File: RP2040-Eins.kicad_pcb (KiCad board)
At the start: 4 copper layers, 68.6 x 53.3 mm, 61 parts, among them J1 CONN_PWR, J10 CONN_USB, J2 CONN_ICSP, J3 CONN_A, J4 CONN_P, J5 CONN_X, J7 CONN_JTAG, J8 CONN_D1, J9 CONN_D2, Q1 AO3401A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

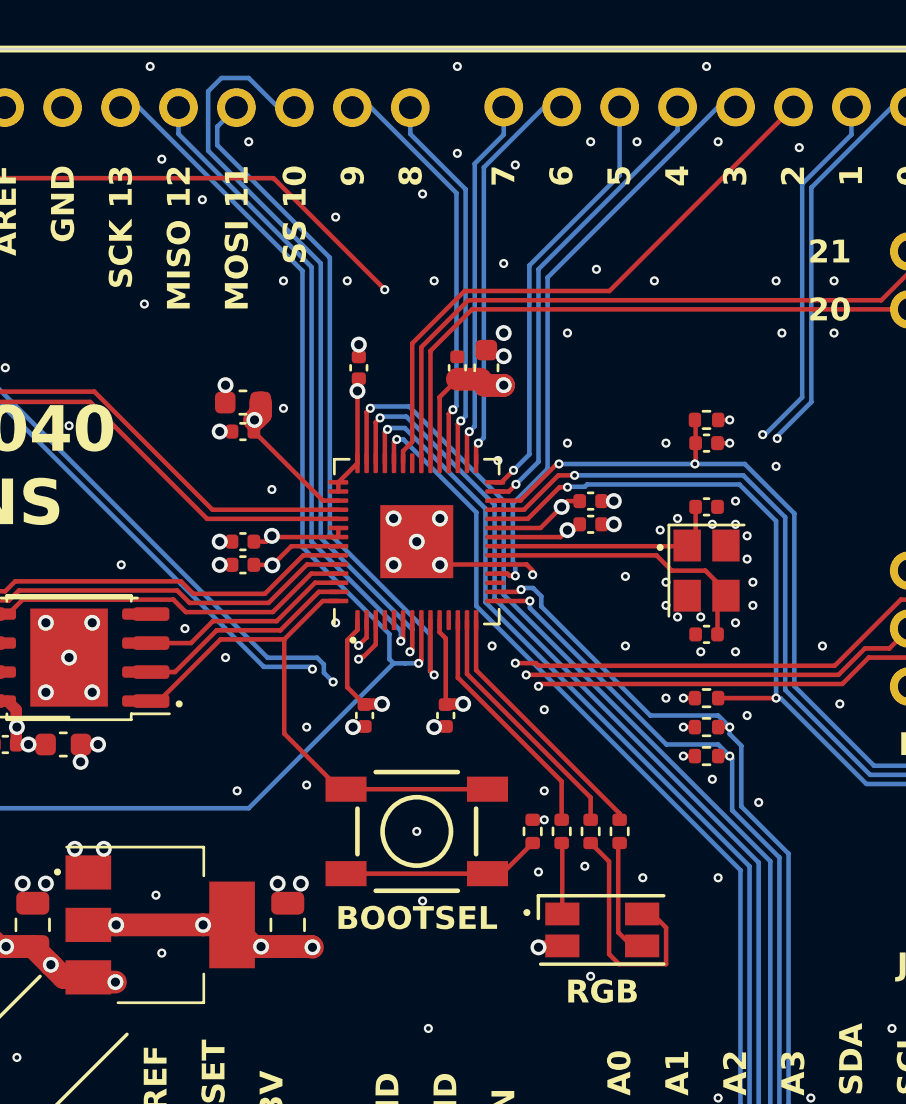
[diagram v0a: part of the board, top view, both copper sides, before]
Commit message: Added mosfets for RGB LED. Moved staff around.
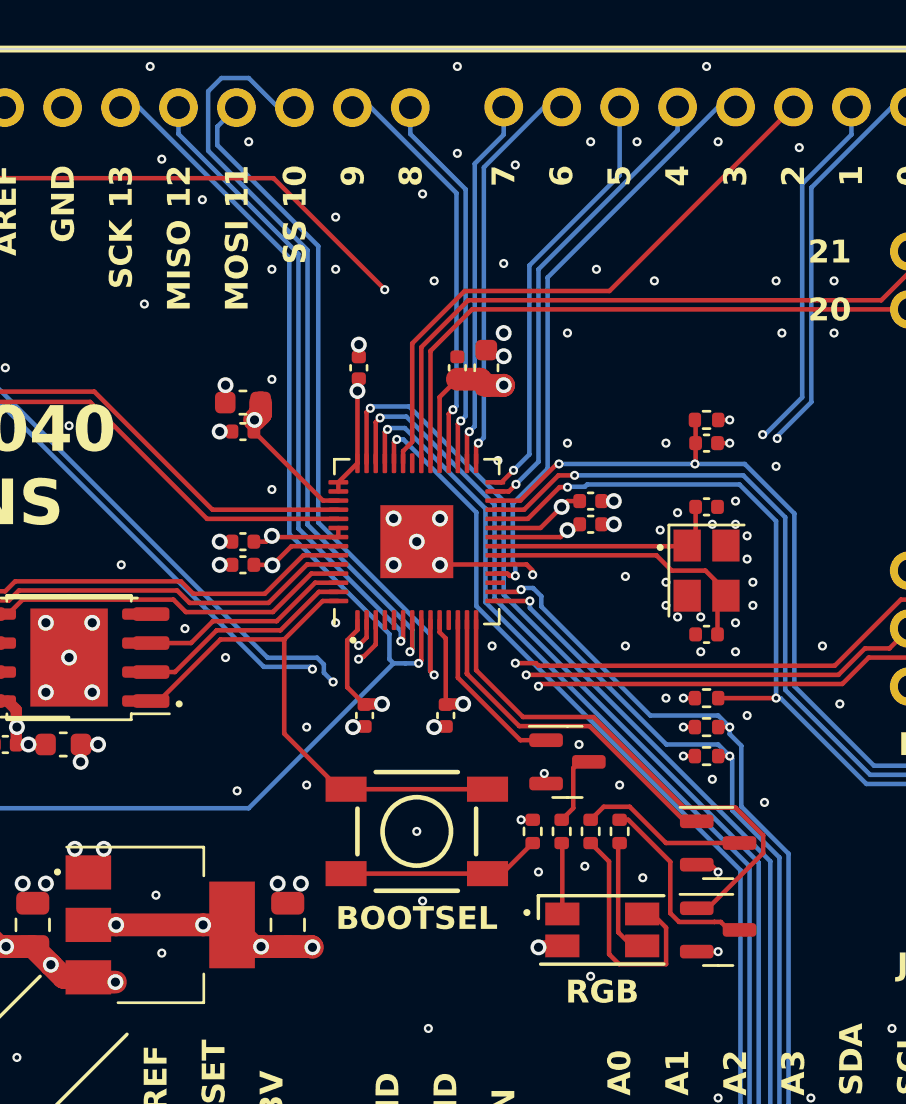
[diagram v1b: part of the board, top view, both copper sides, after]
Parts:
- added Q3: AO3400A, Package_TO_SOT_SMD:SOT-23, F.Cu at (175.5, 104.9)
- added Q4: AO3400A, Package_TO_SOT_SMD:SOT-23, F.Cu at (182.1, 108.5)
- added Q5: AO3400A, Package_TO_SOT_SMD:SOT-23, F.Cu at (182.1, 112.3)
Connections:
- R13 pad 1: LED_R -> Net-(Q3-D)
- R14 pad 1: LED_G -> Net-(Q4-D)
- R15 pad 1: LED_B -> Net-(Q5-D)
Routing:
- net LED_B: track 11.4 -> 22.2 mm
- net Net-(Q5-D): track 0.00 -> 8.57 mm
- net Net-(Q4-D): track 0.00 -> 7.42 mm
- net LED_G: track 11.0 -> 15.1 mm
- net Net-(Q3-D): track 0.00 -> 3.27 mm
- net LED_R: track 10.6 -> 7.53 mm
- net GND: track 10.7 -> 12.9 mm, vias 192 -> 194

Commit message: Moves few stuff around
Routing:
- net GND: vias 194 -> 195

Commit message: Moved stuff around.
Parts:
- moved Q2 22.8 mm to (162.3, 104.9), turned to 180 degrees
- turned Q5 to 180 degrees
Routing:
- net D13_SCK: track 90.6 -> 65.9 mm
- net Net-(D1-K): track 10.7 -> 33.2 mm, vias 0 -> 2
- net Net-(Q5-D): track 8.57 -> 6.70 mm
- net LED_B: track 22.2 -> 23.3 mm
- net GND: track 12.9 -> 13.9 mm, vias 195 -> 209

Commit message: Added QR Code on the back side.
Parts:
- added G***: LOGO, LOGO, B.Cu at (173.2, 114.0)

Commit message: Moved stuff around.
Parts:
- G1: renamed from G***; value LOGO -> QR-CODE
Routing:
- net GND: vias 209 -> 212

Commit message: Moved stuff around.
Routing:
- net GND: vias 212 -> 213
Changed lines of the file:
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@@
   (title_block
     (title "RP2040-Eins-0010")
-    (date "2023-11-03")
+    (date "2023-11-04")
     (rev "1.0")
     (company "(c) 2023 Andriy Golovnya")
@@
       (viasonmask false)
       (mode 1)
-      (useauxorigin false)
+      (useauxorigin true)
       (hpglpennumber 1)
       (hpglpenspeed 20)
@@
   (via (at 140.208 110.49) (size 0.7) (drill 0.4) (layers "F.Cu" "B.Cu") (free) (net 4))
   (via (at 179.834184 107.61333) (size 0.4) (drill 0.2) (layers "F.Cu" "B.Cu") (free) (net 4))
+  (via (at 171.45 103.505) (size 0.4) (drill 0.2) (layers "F.Cu" "B.Cu") (free) (net 4))
   (via (at 160.274 90.424) (size 0.7) (drill 0.4) (layers "F.Cu" "B.Cu") (free) (net 4))
   (via (at 156.464 121.412) (size 0.4) (drill 0.2) (layers "F.Cu" "B.Cu") (free) (net 4))
@@
   (segment (start 169.11 86.725686) (end 171.165687 84.67) (width 0.2) (layer "F.Cu") (net 30))
   (segment (start 169.11 91.8125) (end 169.11 86.725686) (width 0.2) (layer "F.Cu") (net 30))
+  (segment (start 136.0975 95.504) (end 135.795768 95.202268) (width 1) (layer "F.Cu") (net 31))
+  (segment (start 135.795768 91.735768) (end 135.636 91.576) (width 1) (layer "F.Cu") (net 31))
   (segment (start 134.420498 86.45) (end 133.585 86.45) (width 0.5) (layer "F.Cu") (net 31))
   (segment (start 136.67345 87.94455) (end 136.718 87.9) (width 0.5) (layer "F.Cu") (net 31))
   (segment (start 135.636 91.576) (end 135.41 91.35) (width 0.5) (layer "F.Cu") (net 31))
-  (segment (start 136.0975 95.504) (end 135.886 95.2925) (width 1) (layer "F.Cu") (net 31))
   (segment (start 135.41 91.35) (end 133.585 91.35) (width 0.5) (layer "F.Cu") (net 31))
   (segment (start 135.987982 87.94455) (end 136.67345 87.94455) (width 0.5) (layer "F.Cu") (net 31))
-  (segment (start 135.886 95.2925) (end 135.886 91.826) (width 1) (layer "F.Cu") (net 31))
+  (segment (start 135.795768 95.202268) (end 135.795768 91.735768) (width 1) (layer "F.Cu") (net 31))
   (segment (start 134.859502 86.889004) (end 134.420498 86.45) (width 0.5) (layer "F.Cu") (net 31))
-  (segment (start 135.886 91.826) (end 135.636 91.576) (width 1) (layer "F.Cu") (net 31))
   (segment (start 134.859502 87.0005) (end 134.859502 86.889004) (width 0.5) (layer "F.Cu") (net 31))
   (via (at 134.859502 87.0005) (size 0.7) (drill 0.4) (layers "F.Cu" "B.Cu") (net 31))
@@
         (xy 194.867834 119.916701)
         (xy 194.92561 119.65111)
-        (xy 194.945 119.38)
       )
     )
@@
         (xy 194.867834 91.976701)
         (xy 194.92561 91.71111)
-        (xy 194.945 91.44)
       )
     )
@@
         (xy 142.797834 124.996701)
         (xy 142.85561 124.73111)
-        (xy 142.875 124.46)
       )
     )
@@
         (xy 144.067834 76.736701)
         (xy 144.12561 76.47111)
-        (xy 144.145 76.2)
       )
     )

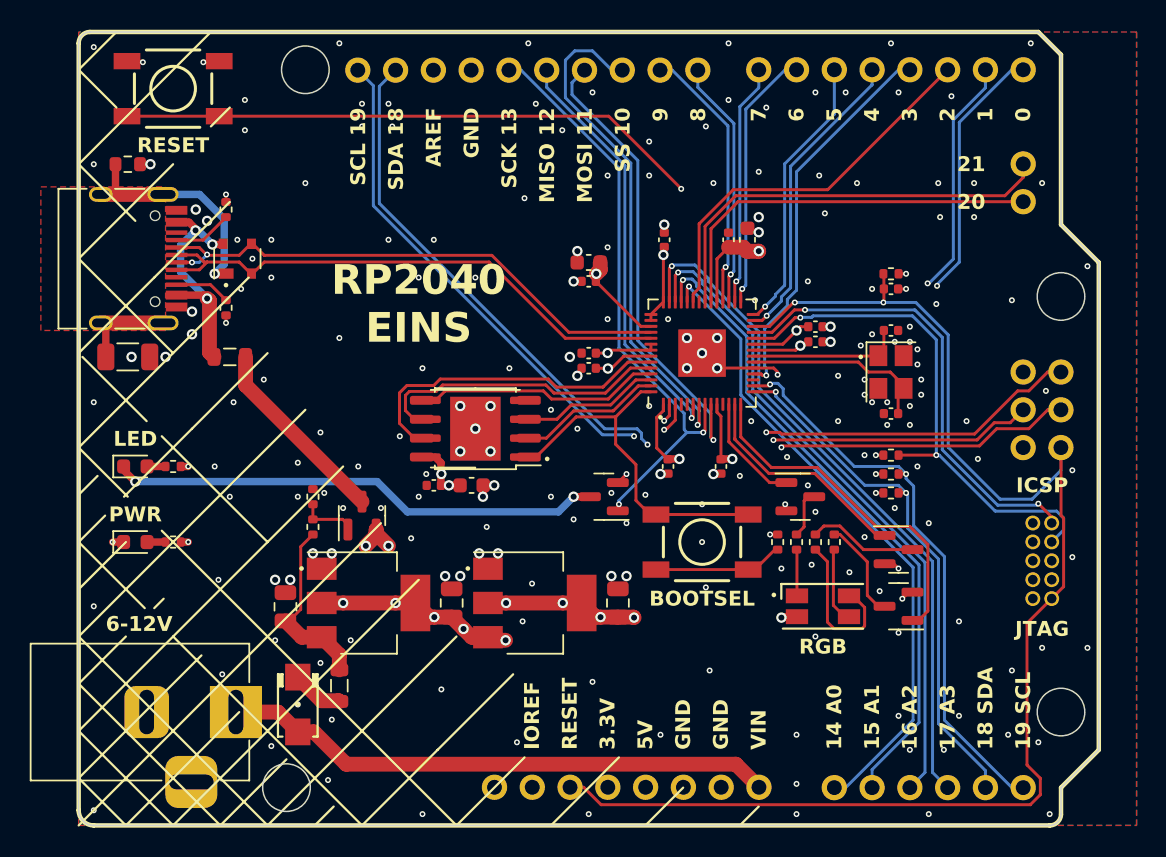
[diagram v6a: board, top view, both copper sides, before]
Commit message: Moved BOOTSEL button closer to the front edge of the board. Moved stuff around to fit better.
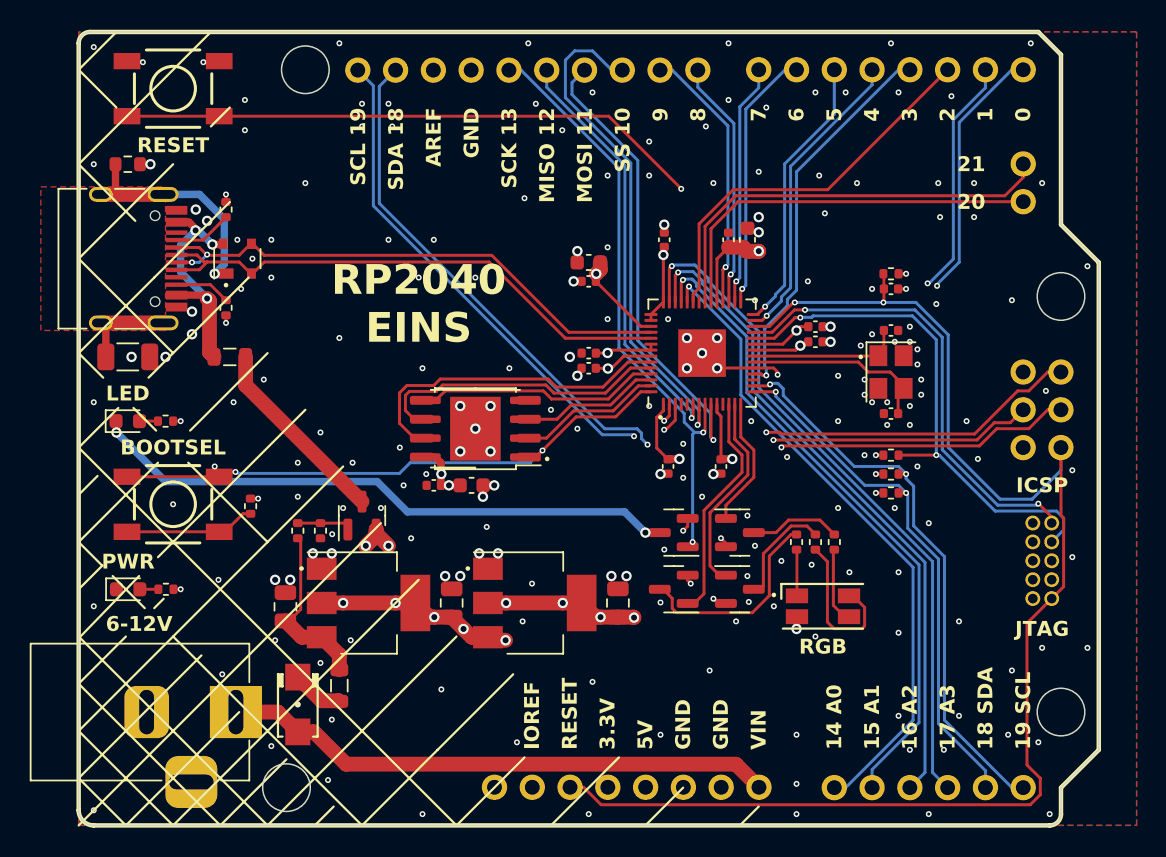
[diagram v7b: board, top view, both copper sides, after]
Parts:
- moved SW1 35.7 mm to (133.3, 105.4)
- moved R7 35.5 mm to (138.6, 105.5)
- moved Q5 11.8 mm to (171.4, 107.3), turned to 0 degrees
- moved Q4 11.0 mm to (171.4, 111.1)
- moved Q3 10.5 mm to (167.0, 111.1), turned to 180 degrees
- moved Q2 5.28 mm to (167.0, 107.3)
- moved D2 3.21 mm to (130.3, 111.1)
- moved R6 3.21 mm to (132.9, 111.1)
- moved D1 3.09 mm to (130.3, 99.8)
- moved R1 3.09 mm to (132.8, 99.8)
- moved R9 2.34 mm to (143.3, 107.2), turned to -90 degrees
- moved R8 1.05 mm to (141.7, 107.2)
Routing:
- net LED_B: track 23.5 -> 8.82 mm
- net QSPI_SS: track 24.1 -> 38.8 mm, vias 0 -> 2
- net Net-(Q3-D): track 3.27 -> 14.0 mm
- net LED_R: track 7.53 -> 15.5 mm
- net Net-(D1-K): track 33.2 -> 40.1 mm
- net LED_G: track 15.1 -> 13.7 mm
- net GND: track 13.9 -> 13.2 mm, vias 213 -> 212
- net Net-(Q5-D): track 6.70 -> 6.16 mm
- net VPWR: track 12.3 -> 11.8 mm

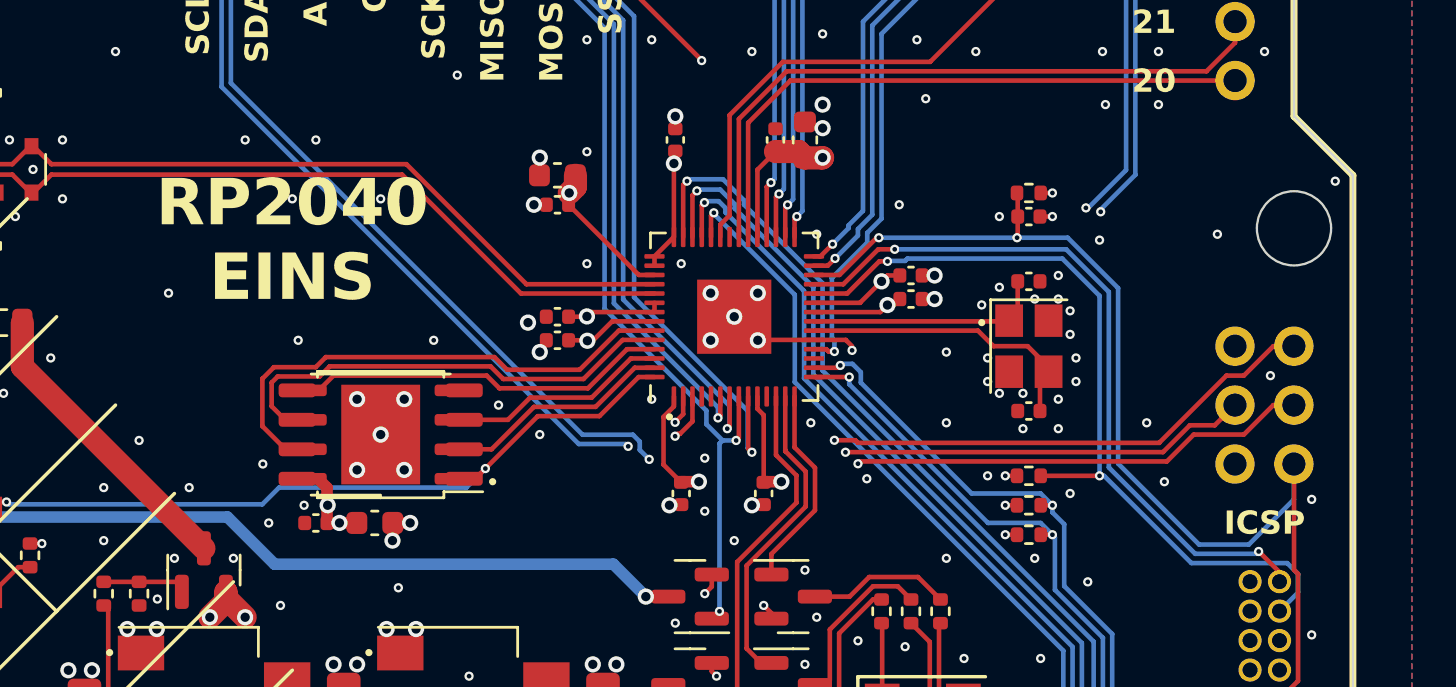
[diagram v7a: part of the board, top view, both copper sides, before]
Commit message: Added fancy label. Moved some texts around.
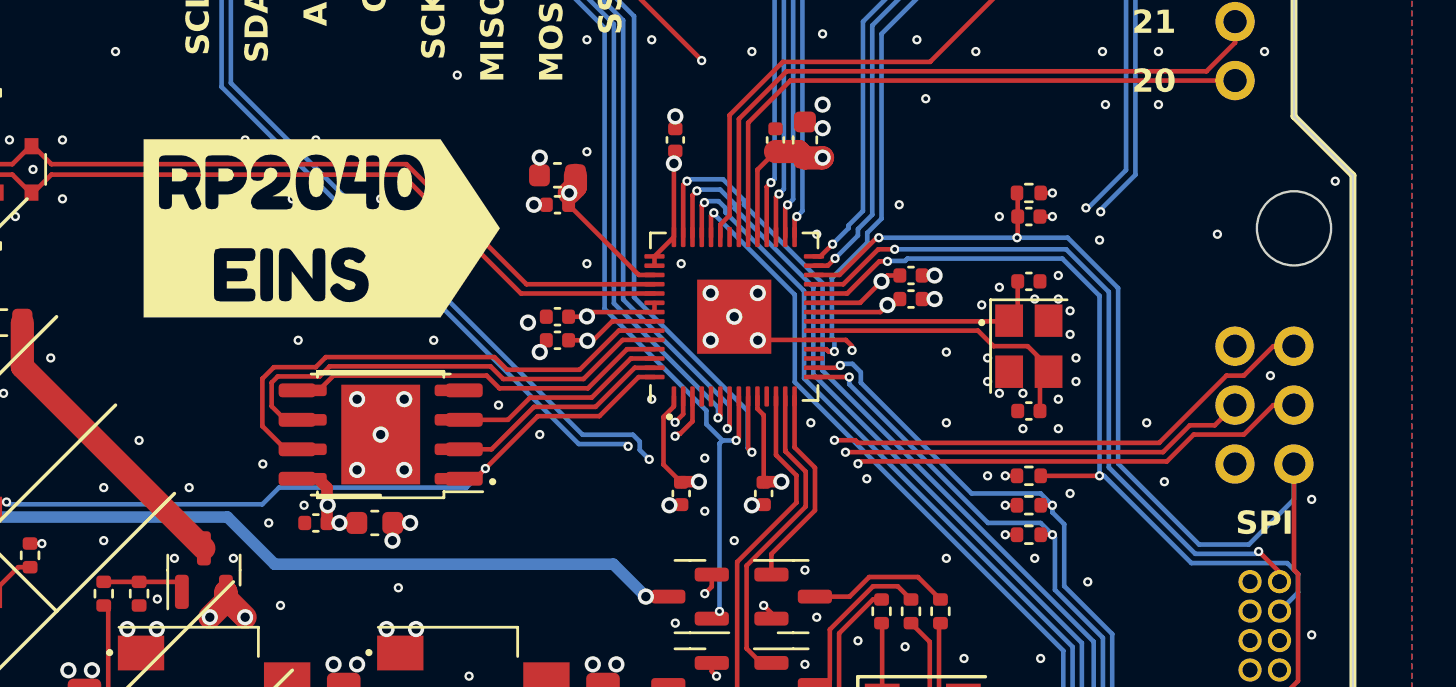
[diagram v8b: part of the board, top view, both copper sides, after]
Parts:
- added G2: BOARD-LABEL, kibuzzard-654A67CC, F.Cu at (151.1, 91.4)
- moved G1 3.56 mm to (173.2, 110.5)
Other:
- board text added: "SPI"
- board text removed: "ICSP"
- board text removed: "RP2040 EINS"
